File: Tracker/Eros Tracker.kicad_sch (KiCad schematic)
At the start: 0 parts

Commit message: Midway through board layout
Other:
- sheet Eros Tracker Connectors ports: added +EXT_MOTOR, -EXT_MOTOR, I2C_SCL, I2C_SDA, INT, POWER_VIN1, POWER_VIN2, VBUS_OUT, ~{RESET}; removed none
- sheet Eros Tracker Microcontroller ports: added +EXT_MOTOR, -EXT_MOTOR, ENABLE, ~{BAT_STAT_CHARGING}; removed LED, PWR_LATCH, VBATT_MON, ~{BUTTON_INPUT}
- sheet Eros Tracker Power & Battery ports: added POWER_VIN1, POWER_VIN2, VBUS_OUT, ~{BAT_STAT_CHARGING}, ~{BAT_STAT_CHRG_DONE}; removed PWR_LATCH, ~{BUTTON_INPUT}

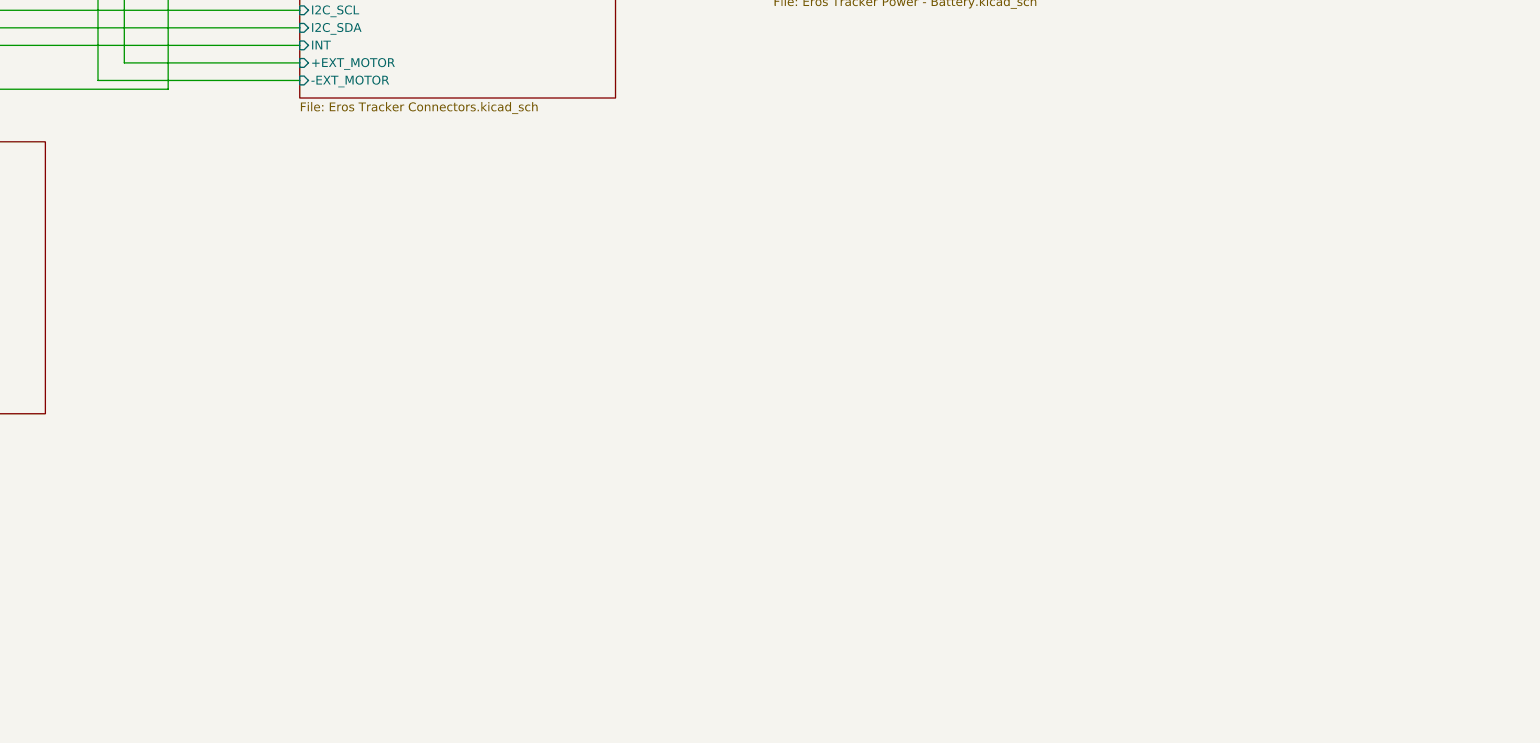
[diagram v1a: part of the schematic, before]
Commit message: Added cuts and jumps for Rev A
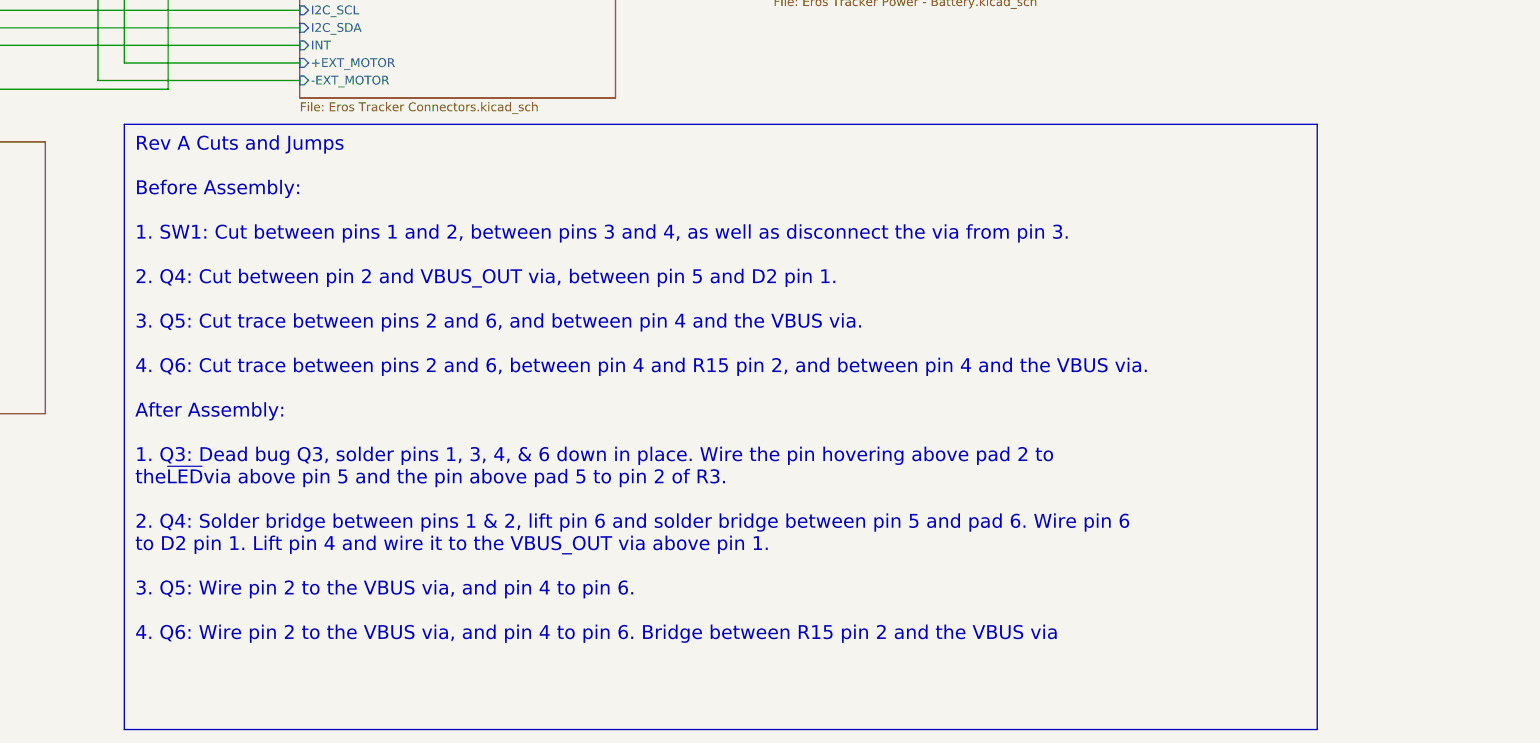
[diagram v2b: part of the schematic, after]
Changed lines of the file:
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@@
     (stroke (width 0) (type default))
+  )
+  (text_box "Rev A Cuts and Jumps\n\nBefore Assembly:\n\n1. SW1: Cut between pins 1 and 2, between pins 3 and 4, as well as disconnect the via from pin 3.\n\n2. Q4: Cut between pin 2 and VBUS_OUT via, between pin 5 and D2 pin 1.\n\n3. Q5: Cut trace between pins 2 and 6, and between pin 4 and the VBUS via.\n\n4. Q6: Cut trace between pins 2 and 6, between pin 4 and R15 pin 2, and between pin 4 and the VBUS via.\n\nAfter Assembly:\n\n1. Q3: Dead bug Q3, solder pins 1, 3, 4, & 6 down in place. Wire the pin hovering above pad 2 to the~{LED}via above pin 5 and the pin above pad 5 to pin 2 of R3.\n\n2. Q4: Solder bridge between pins 1 & 2, lift pin 6 and solder bridge between pin 5 and pad 6. Wire pin 6 to D2 pin 1. Lift pin 4 and wire it to the VBUS_OUT via above pin 1.\n\n3. Q5: Wire pin 2 to the VBUS via, and pin 4 to pin 6.\n\n4. Q6: Wire pin 2 to the VBUS via, and pin 4 to pin 6. Bridge between R15 pin 2 and the VBUS via"
+    (at 111.76 119.38 0) (size 172.72 87.63)
+    (stroke (width 0) (type default))
+    (fill (type none))
+    (effects (font (size 2 2)) (justify left top))
   )
   (symbol (lib_id "power:GND") (at 57.15 152.4 270) (unit 1)

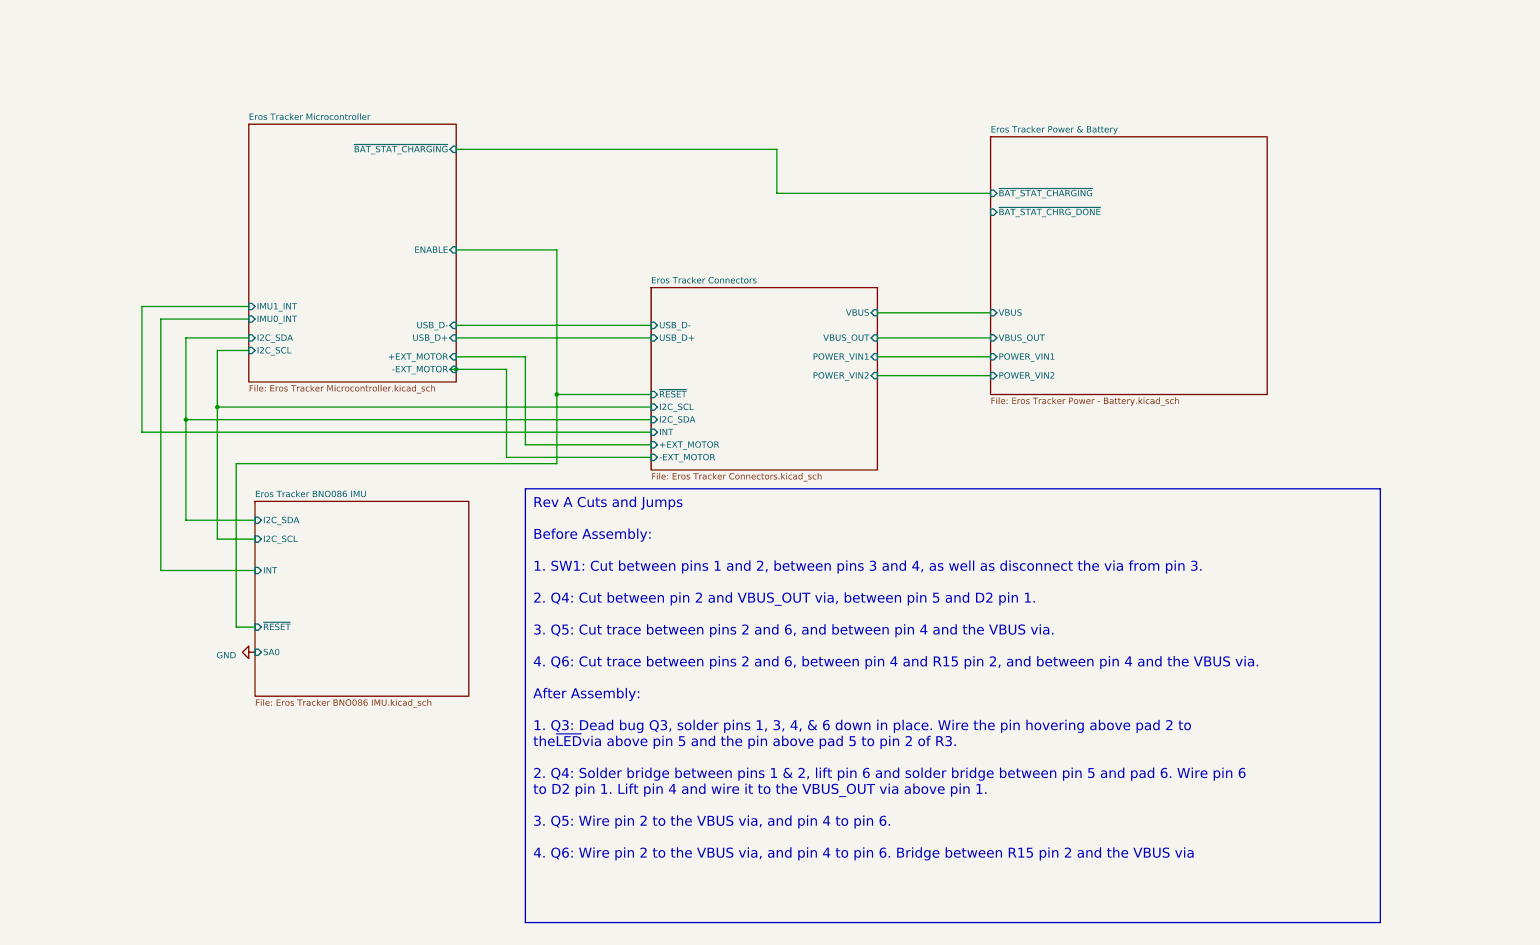
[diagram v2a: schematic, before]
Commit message: RevC release. Power passthrough, battery voltage monitoring, IMU interrupt line fixed. TVS diodes added to all human-reachable connections.
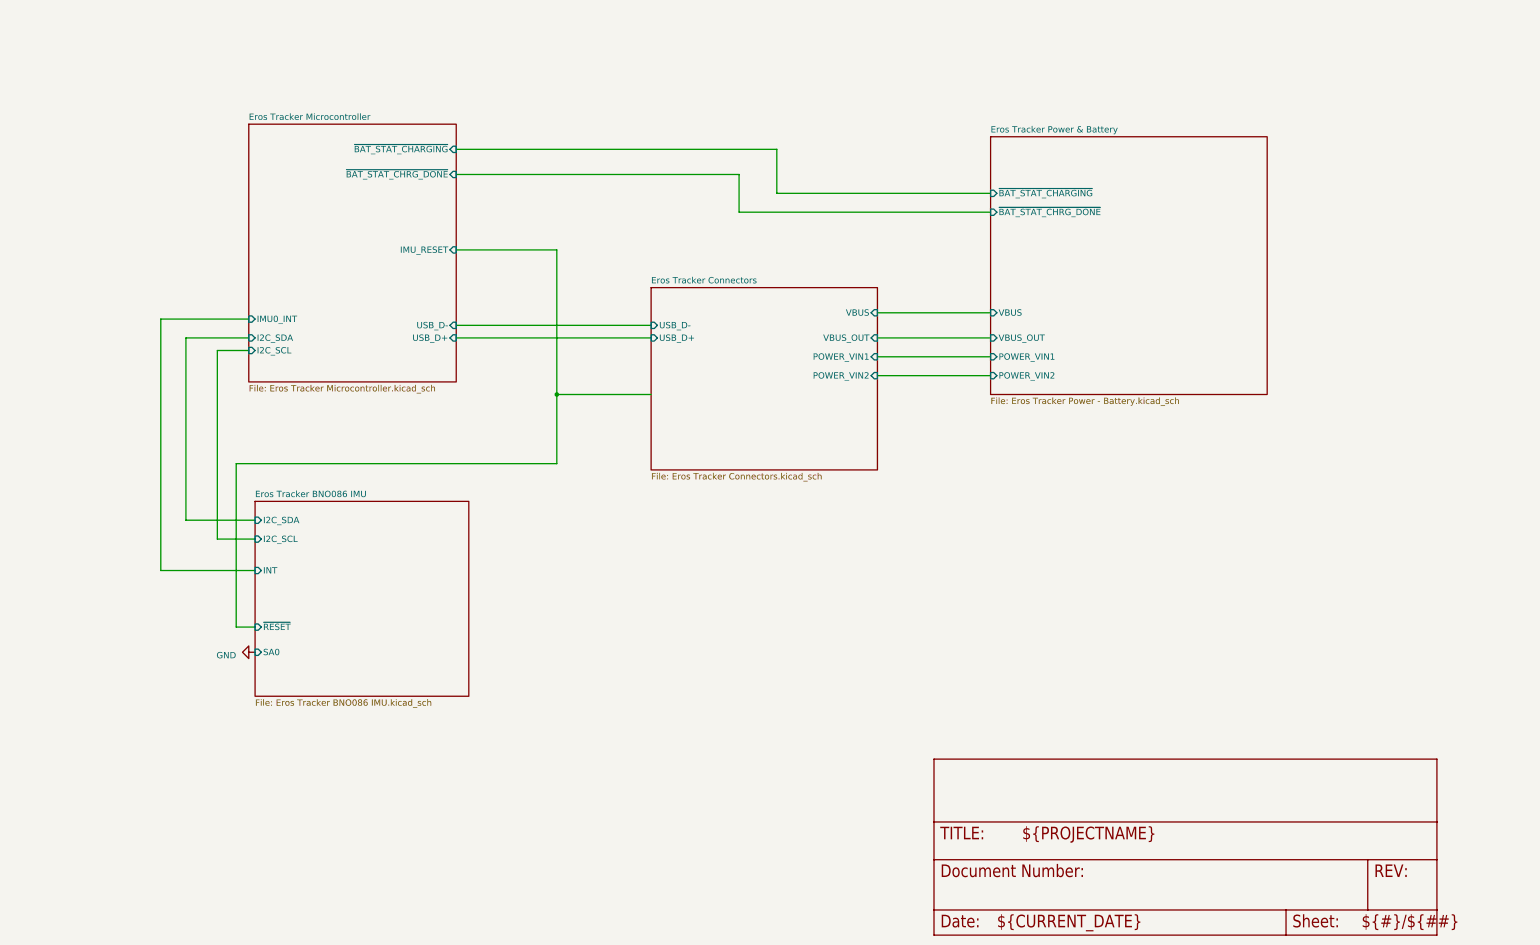
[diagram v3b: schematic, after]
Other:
- sheet Eros Tracker Connectors ports: added none; removed +EXT_MOTOR, -EXT_MOTOR, I2C_SCL, I2C_SDA, INT, ~{RESET}
- sheet Eros Tracker Microcontroller ports: added IMU_RESET, ~{BAT_STAT_CHRG_DONE}; removed +EXT_MOTOR, -EXT_MOTOR, ENABLE, IMU1_INT
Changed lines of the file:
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@@
 (kicad_sch (version 20230121) (generator eeschema)
   (paper "A4")
-  (junction (at 43.18 105.41) (diameter 0) (color 0 0 0 0)
-  )
   (junction (at 118.11 100.33) (diameter 0) (color 0 0 0 0)
   )
-  (junction (at 49.53 102.87) (diameter 0) (color 0 0 0 0)
-  )
-  (junction (at 97.79 95.25) (diameter 0) (color 0 0 0 0)
-  )
-  (wire (pts (xy 49.53 102.87) (xy 49.53 129.54))
-    (stroke (width 0) (type default))
-  )
-  (wire (pts (xy 34.29 107.95) (xy 34.29 82.55))
+  (wire (pts (xy 49.53 91.44) (xy 49.53 129.54))
     (stroke (width 0) (type default))
   )
@@
     (stroke (width 0) (type default))
   )
+  (wire (pts (xy 154.94 63.5) (xy 205.74 63.5))
+    (stroke (width 0) (type default))
+  )
   (wire (pts (xy 118.11 114.3) (xy 118.11 100.33))
     (stroke (width 0) (type default))
@@
     (stroke (width 0) (type default))
   )
-  (wire (pts (xy 107.95 95.25) (xy 107.95 113.03))
-    (stroke (width 0) (type default))
-  )
-  (wire (pts (xy 43.18 105.41) (xy 43.18 125.73))
+  (wire (pts (xy 43.18 88.9) (xy 43.18 125.73))
     (stroke (width 0) (type default))
   )
@@
     (stroke (width 0) (type default))
   )
-  (wire (pts (xy 43.18 88.9) (xy 43.18 105.41))
-    (stroke (width 0) (type default))
-  )
-  (wire (pts (xy 137.16 110.49) (xy 111.76 110.49))
-    (stroke (width 0) (type default))
-  )
   (wire (pts (xy 97.79 86.36) (xy 137.16 86.36))
     (stroke (width 0) (type default))
@@
     (stroke (width 0) (type default))
   )
+  (wire (pts (xy 97.79 55.88) (xy 154.94 55.88))
+    (stroke (width 0) (type default))
+  )
+  (wire (pts (xy 154.94 55.88) (xy 154.94 63.5))
+    (stroke (width 0) (type default))
+  )
   (wire (pts (xy 49.53 129.54) (xy 57.15 129.54))
     (stroke (width 0) (type default))
   )
-  (wire (pts (xy 96.52 95.25) (xy 97.79 95.25))
-    (stroke (width 0) (type default))
-  )
-  (wire (pts (xy 49.53 91.44) (xy 49.53 102.87))
-    (stroke (width 0) (type default))
-  )
   (wire (pts (xy 182.88 96.52) (xy 205.74 96.52))
     (stroke (width 0) (type default))
@@
     (stroke (width 0) (type default))
   )
-  (wire (pts (xy 107.95 113.03) (xy 137.16 113.03))
-    (stroke (width 0) (type default))
-  )
   (wire (pts (xy 43.18 125.73) (xy 57.15 125.73))
     (stroke (width 0) (type default))
   )
-  (wire (pts (xy 43.18 105.41) (xy 137.16 105.41))
-    (stroke (width 0) (type default))
-  )
   (wire (pts (xy 97.79 88.9) (xy 137.16 88.9))
     (stroke (width 0) (type default))
   )
-  (wire (pts (xy 34.29 82.55) (xy 55.88 82.55))
-    (stroke (width 0) (type default))
-  )
   (wire (pts (xy 38.1 85.09) (xy 38.1 135.89))
     (stroke (width 0) (type default))
   )
-  (wire (pts (xy 97.79 95.25) (xy 107.95 95.25))
-    (stroke (width 0) (type default))
-  )
-  (wire (pts (xy 111.76 110.49) (xy 111.76 92.71))
-    (stroke (width 0) (type default))
-  )
-  (wire (pts (xy 49.53 102.87) (xy 137.16 102.87))
-    (stroke (width 0) (type default))
-  )
-  (wire (pts (xy 137.16 107.95) (xy 34.29 107.95))
-    (stroke (width 0) (type default))
-  )
   (wire (pts (xy 205.74 59.69) (xy 162.56 59.69))
     (stroke (width 0) (type default))
@@
     (stroke (width 0) (type default))
   )
-  (wire (pts (xy 111.76 92.71) (xy 97.79 92.71))
-    (stroke (width 0) (type default))
-  )
   (wire (pts (xy 182.88 88.9) (xy 205.74 88.9))
     (stroke (width 0) (type default))
@@
   (wire (pts (xy 182.88 92.71) (xy 205.74 92.71))
     (stroke (width 0) (type default))
-  )
-  (text_box "Rev A Cuts and Jumps\n\nBefore Assembly:\n\n1. SW1: Cut between pins 1 and 2, between pins 3 and 4, as well as disconnect the via from pin 3.\n\n2. Q4: Cut between pin 2 and VBUS_OUT via, between pin 5 and D2 pin 1.\n\n3. Q5: Cut trace between pins 2 and 6, and between pin 4 and the VBUS via.\n\n4. Q6: Cut trace between pins 2 and 6, between pin 4 and R15 pin 2, and between pin 4 and the VBUS via.\n\nAfter Assembly:\n\n1. Q3: Dead bug Q3, solder pins 1, 3, 4, & 6 down in place. Wire the pin hovering above pad 2 to the~{LED}via above pin 5 and the pin above pad 5 to pin 2 of R3.\n\n2. Q4: Solder bridge between pins 1 & 2, lift pin 6 and solder bridge between pin 5 and pad 6. Wire pin 6 to D2 pin 1. Lift pin 4 and wire it to the VBUS_OUT via above pin 1.\n\n3. Q5: Wire pin 2 to the VBUS via, and pin 4 to pin 6.\n\n4. Q6: Wire pin 2 to the VBUS via, and pin 4 to pin 6. Bridge between R15 pin 2 and the VBUS via"
-    (at 111.76 119.38 0) (size 172.72 87.63)
-    (stroke (width 0) (type default))
-    (fill (type none))
-    (effects (font (size 2 2)) (justify left top))
   )
   (symbol (lib_id "power:GND") (at 57.15 152.4 270) (unit 1)
@@
     )
   )
+  (symbol (lib_id "Eros Tracker-eagle-import:FRAME_A_L") (at 194.31 209.55 0) (unit 2)
+    (in_bom yes) (on_board yes) (dnp no)
+    (property "Reference" "#FRAME2" (at 194.31 209.55 0)
+      (effects (font (size 1.27 1.27)) hide)
+    )
+    (property "Value" "FRAME_A_L" (at 194.31 209.55 0)
+      (effects (font (size 1.27 1.27)) hide)
+    )
+    (property "Footprint" "" (at 194.31 209.55 0)
+      (effects (font (size 1.27 1.27)) hide)
+    )
+    (property "Datasheet" "" (at 194.31 209.55 0)
+      (effects (font (size 1.27 1.27)) hide)
+    )
+    (instances
+      (project "Eros Tracker"
+        (path "/e762b1f0-85b9-427f-b9a8-4b9d5ef7d00a/576653f3-b0de-4b89-84c9-67e946662380"
+          (reference "#FRAME2") (unit 2)
+        )
+        (path "/e762b1f0-85b9-427f-b9a8-4b9d5ef7d00a"
+          (reference "#FRAME5") (unit 2)
+        )
+      )
+    )
+  )
   (sheet (at 57.15 121.92) (size 43.18 39.37) (fields_autoplaced)
     (stroke (width 0.1524) (type solid))
@@
       (effects (font (size 1.27 1.27)) (justify right))
     )
-    (pin "IMU1_INT" input (at 55.88 82.55 180)
-      (effects (font (size 1.27 1.27)) (justify left))
-    )
-    (pin "ENABLE" input (at 97.79 71.12 0)
-      (effects (font (size 1.27 1.27)) (justify right))
-    )
-    (pin "+EXT_MOTOR" input (at 97.79 92.71 0)
-      (effects (font (size 1.27 1.27)) (justify right))
-    )
-    (pin "-EXT_MOTOR" input (at 97.79 95.25 0)
-      (effects (font (size 1.27 1.27)) (justify right))
-    )
     (pin "~{BAT_STAT_CHARGING}" input (at 97.79 50.8 0)
+      (effects (font (size 1.27 1.27)) (justify right))
+    )
+    (pin "~{BAT_STAT_CHRG_DONE}" input (at 97.79 55.88 0)
+      (effects (font (size 1.27 1.27)) (justify right))
+    )
+    (pin "IMU_RESET" input (at 97.79 71.12 0)
       (effects (font (size 1.27 1.27)) (justify right))
     )
@@
       (effects (font (size 1.27 1.27)) (justify right))
     )
-    (pin "~{RESET}" input (at 137.16 100.33 180)
-      (effects (font (size 1.27 1.27)) (justify left))
-    )
-    (pin "I2C_SCL" input (at 137.16 102.87 180)
-      (effects (font (size 1.27 1.27)) (justify left))
-    )
-    (pin "I2C_SDA" input (at 137.16 105.41 180)
-      (effects (font (size 1.27 1.27)) (justify left))
-    )
-    (pin "INT" input (at 137.16 107.95 180)
-      (effects (font (size 1.27 1.27)) (justify left))
-    )
     (pin "POWER_VIN1" input (at 182.88 92.71 0)
       (effects (font (size 1.27 1.27)) (justify right))
@@
       (effects (font (size 1.27 1.27)) (justify right))
     )
-    (pin "-EXT_MOTOR" input (at 137.16 113.03 180)
-      (effects (font (size 1.27 1.27)) (justify left))
-    )
-    (pin "+EXT_MOTOR" input (at 137.16 110.49 180)
-      (effects (font (size 1.27 1.27)) (justify left))
-    )
-    (instances
+    (instances
